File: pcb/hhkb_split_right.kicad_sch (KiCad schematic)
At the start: 82 parts, among them SW1 keyswitch, SW10 keyswitch, SW11 keyswitch, SW12 keyswitch, SW13 keyswitch, SW14 keyswitch, SW15 keyswitch, SW16 keyswitch, SW17 keyswitch, SW18 keyswitch, SW19 keyswitch, SW2 keyswitch, SW20 keyswitch, SW21 keyswitch, SW22 keyswitch, SW23 keyswitch, SW24 keyswitch, SW25 keyswitch, SW26 keyswitch, SW27 keyswitch, SW28 keyswitch, SW29 keyswitch, SW3 keyswitch, SW30 keyswitch, SW31 keyswitch, SW32 keyswitch, SW33 keyswitch, SW34 keyswitch, SW4 keyswitch, SW5 keyswitch, SW6 keyswitch, SW7 keyswitch, SW8 keyswitch, SW9 keyswitch, U1 74LVC595, U2 74LVC595

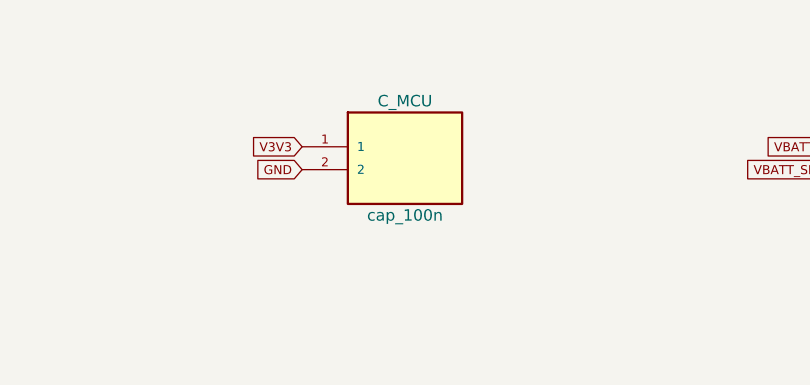
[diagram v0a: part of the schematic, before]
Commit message: ★ パスコンが IC から 17mm 離れていたのを 2.6mm にした（指摘 6）
実測すると **C_U1 の V3V3 パッドは U1 の VCC ピンから 17.0mm** あった。
この距離ではパスコンとして働かない。しかも C_MCU（当時）のほうが U1 に
近いという逆転した並びで、名前と役割も食い違っていた。

原因は PLACE に x を手で書いていたこと。**座標を手で書くのをやめ、
IC の V3V3 パッドがどちら側にあるかを実際の座標から決めて、
コートヤードが触れない最短の位置まで寄せる**ようにした
（gen_pcb.DECOUPLE_BESIDE / _place_beside）。IC の向きを変えても追随する。

  VCC 間  17.0mm → **2.64mm**（左右とも）

GND 間が 9.97mm 残るのは TSSOP-16 の VCC(16) と GND(8) が対角にある
ためで、パッケージの都合。**GND 側の戻りは地板で受ける**——だから
指摘 4（GND ビアを多く）が効く。

C_MCU → C_RAIL に改名した。**この基板に MCU は無い**（XIAO は子基板側で、
そちらには C_DB がある）。名前が役割を偽っていた。実体は「レールが
基板を出入りするところ（J_DB）のパスコン」なので、そう置き直した。

Co-Authored-By: Claude Sonnet 5 <noreply@anthropic.com>
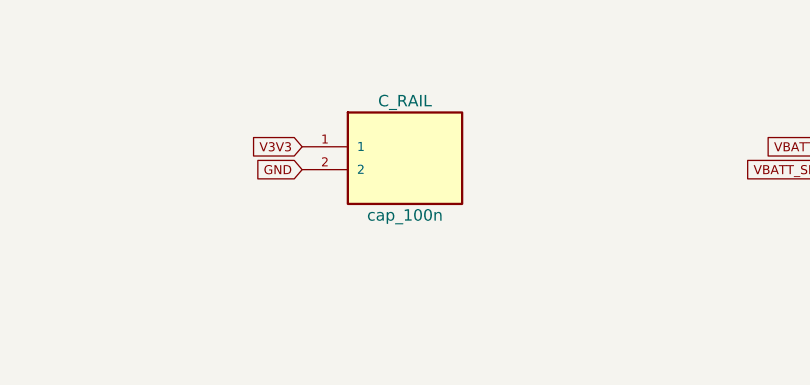
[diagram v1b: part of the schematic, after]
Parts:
- removed C_MCU: cap_100n, symbol hhkb_split_right:cap_100n
- added C_RAIL: cap_100n, symbol hhkb_split_right:cap_100n
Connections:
- net GND: now also C_RAIL.2
- net V3V3: now also C_RAIL.1
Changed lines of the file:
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@@
 		(on_board yes)
 		(dnp no)
-		(property "Reference" "C_MCU" (at 427.99 24.13 0) (effects (font (size 1.27 1.27))))
+		(property "Reference" "C_RAIL" (at 427.99 24.13 0) (effects (font (size 1.27 1.27))))
 		(property "Value" "cap_100n" (at 427.99 36.83 0) (effects (font (size 1.27 1.27))))
 		(pin "1")
@@
 			(project "hhkb_split_right"
 				(path "/68e5bc58-ebc5-5f0d-bfc6-cc94dff2192d"
-					(reference "C_MCU")
+					(reference "C_RAIL")
 					(unit 1)
 				)
